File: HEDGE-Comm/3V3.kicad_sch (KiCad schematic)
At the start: 16 parts, among them U3 A6986F

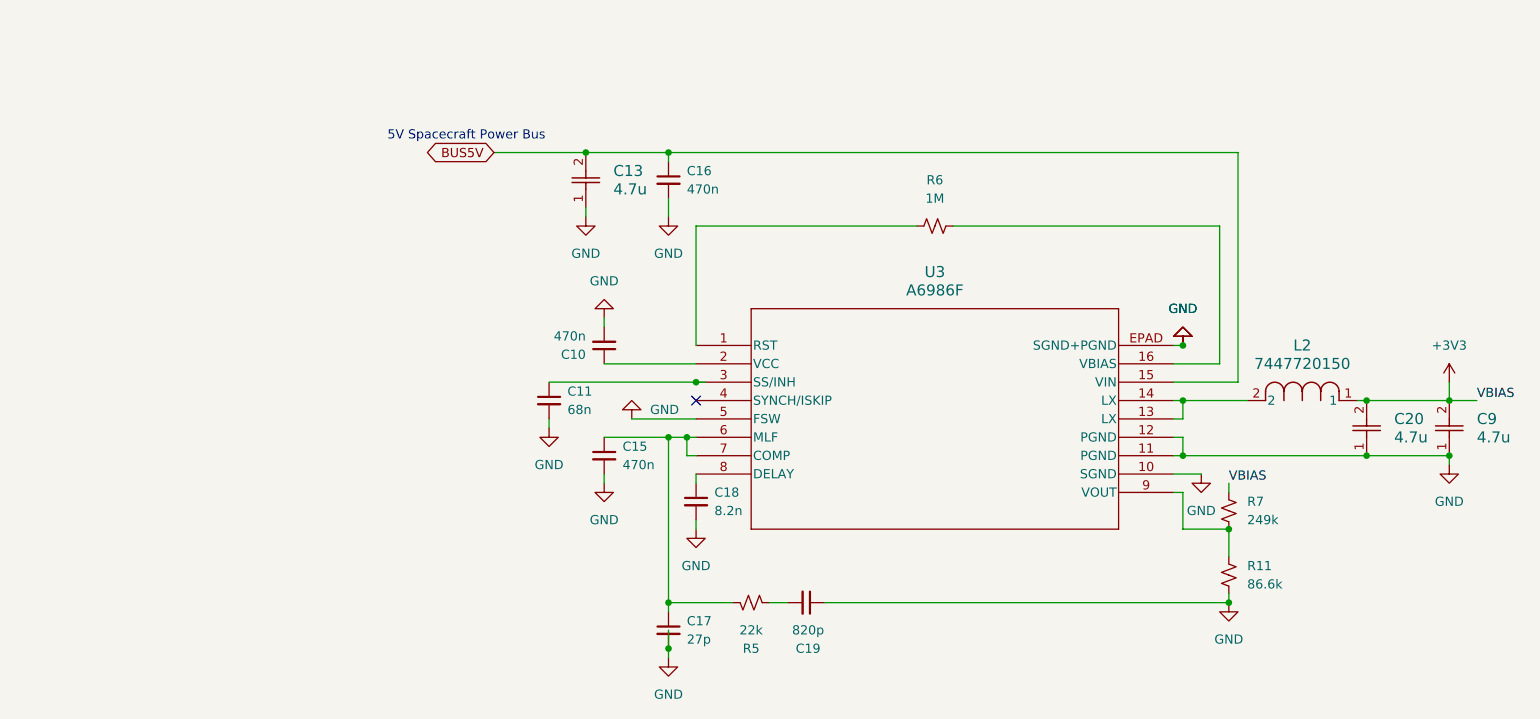
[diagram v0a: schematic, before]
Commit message: Repair KiCAD files; modularize common circuits
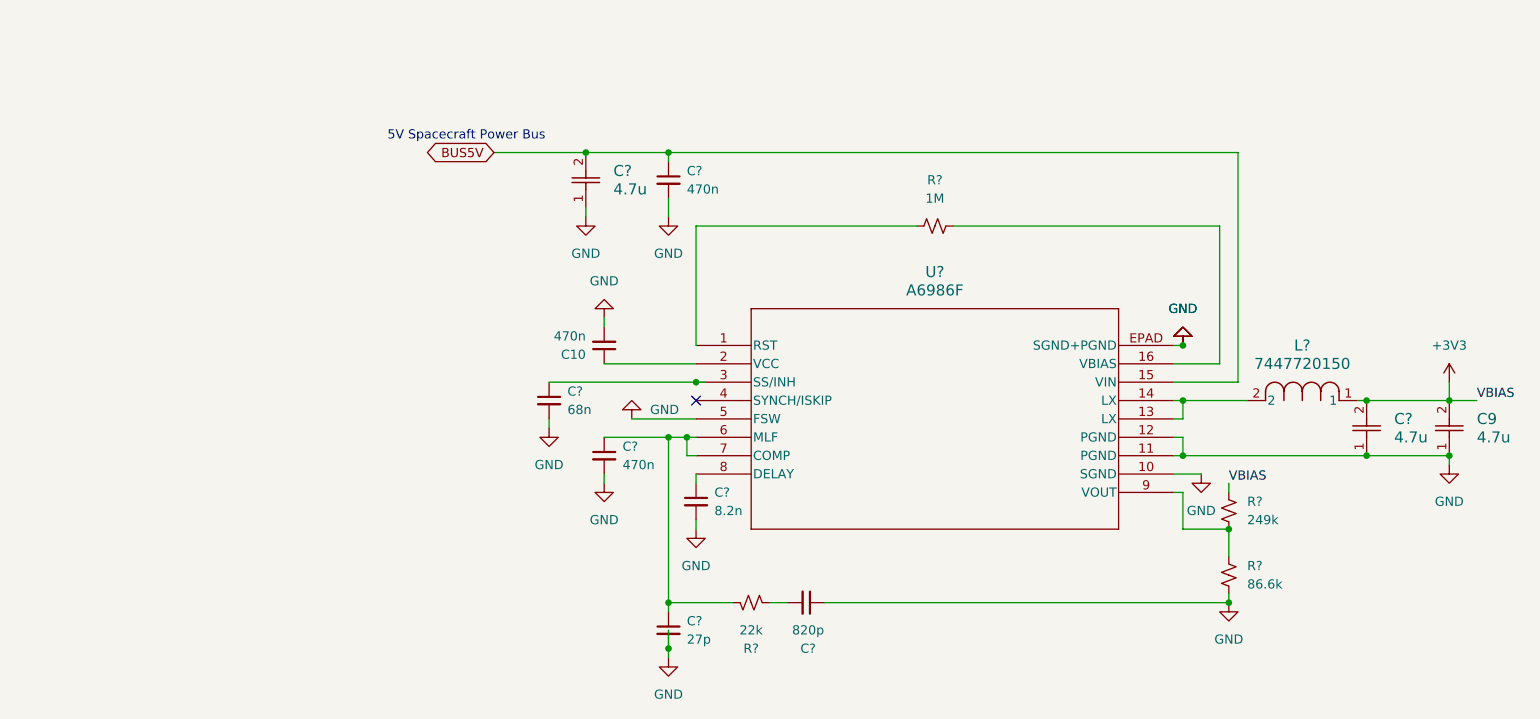
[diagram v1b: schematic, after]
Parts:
- renumbered C16 to C?, C15 to C?, C17 to C?, C19 to C?, C18 to C?, C11 to C?, C13 to C?, C20 to C?, L2 to L?, R11 to R?, R7 to R?, R5 to R?, R6 to R?, U3 to U?

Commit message: Refactor Data PCB files; enter RS485; enter Iridium radio power
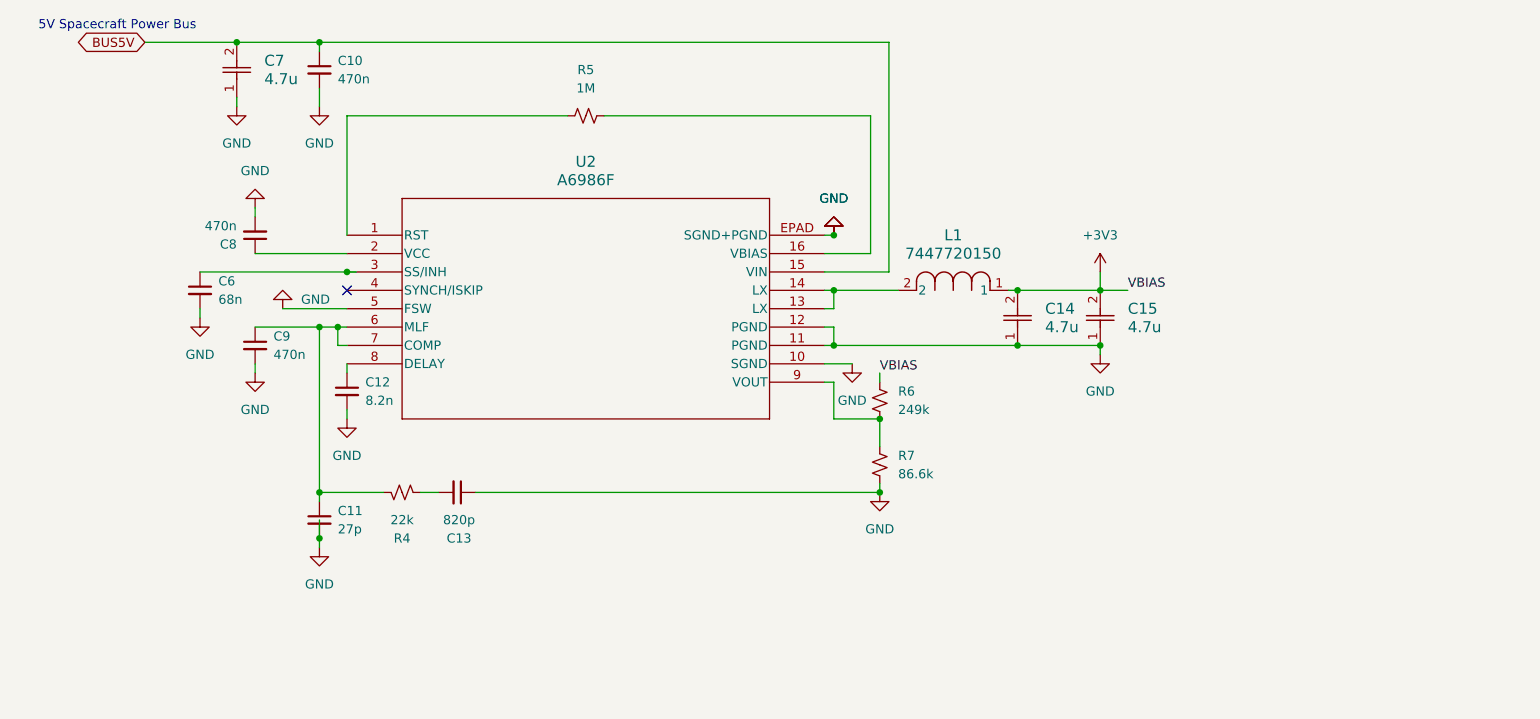
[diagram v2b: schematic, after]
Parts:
- removed C9, C?: 4.7u, CAP_GRM15-5_MUR, symbol Cout:GRM155R60J475ME87D
- removed C? (x2): 470n, symbol Device:C_Small
- removed C?: 27p, symbol Device:C_Small
- removed C?: 820p, symbol Device:C_Small
- removed C?: 8.2n, symbol Device:C_Small
- removed C?: 68n, symbol Device:C_Small
- removed C?: 4.7u, CAP_GRM21_MUR, symbol Cin:GRM219R61A475KE34D
- removed L?: 7447720150, IND_8095-WE-TI_8p3x10x5_WRE, symbol L1:7447720150
- removed R?: 86.6k, symbol Device:R_Small_US
- removed R?: 249k, symbol Device:R_Small_US
- removed R?: 22k, symbol Device:R_Small_US
- removed R?: 1M, symbol Device:R_Small_US
- removed U?: A6986F, HTSSOP_986F_STM, symbol A6986F:A6986F
- added C11: 27p, symbol Device:C_Small
- added C12: 8.2n, symbol Device:C_Small
- added C13: 820p, symbol Device:C_Small
- added C14, C15: 4.7u, CAP_GRM15-5_MUR, symbol Cout:GRM155R60J475ME87D
- added C6: 68n, symbol Device:C_Small
- added C7: 4.7u, CAP_GRM21_MUR, symbol Cin:GRM219R61A475KE34D
- added C8, C9: 470n, symbol Device:C_Small
- added L1: 7447720150, IND_8095-WE-TI_8p3x10x5_WRE, symbol L1:7447720150
- added R4: 22k, symbol Device:R_Small_US
- added R5: 1M, symbol Device:R_Small_US
- added R6: 249k, symbol Device:R_Small_US
- added R7: 86.6k, symbol Device:R_Small_US
- added U2: A6986F, HTSSOP_986F_STM, symbol A6986F:A6986F
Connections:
- net BUS5V: now also C10.1, C7.2, U2.15 (VIN)
- net GND: now also C11.2, C12.2, C13.1, C14.1, C15.1, C6.2, C7.1, C8.2, C9.2, R7.2, U2.10 (SGND), U2.11 (PGND), U2.12 (PGND), U2.5 (FSW), U2.EPAD (SGND+PGND)
- net VBIAS: now also C14.2, C15.2, L1.1, R6.1
- new net: C8.1, U2.2 (VCC)
- new net: R6.2, R7.1, U2.9 (VOUT)
- new net: C11.1, C9.1, R4.1, U2.6 (MLF), U2.7 (COMP)
- new net: C13.2, R4.2
- new net: C6.1, U2.3 (SS/INH)
- new net: L1.2, U2.13 (LX), U2.14 (LX)
- new net: R5.1, U2.1 (RST)
- new net: R5.2, U2.16 (VBIAS)
- new net: C12.1, U2.8 (DELAY)
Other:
- company: (none) -> Spacecraft Design Lab
- title: (none) -> HEDGE Comm PCB
